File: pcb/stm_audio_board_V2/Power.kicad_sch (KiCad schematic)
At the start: 25 parts, among them J1 Power conn, U2 AMS1117-3.3, U4 OP275, U5 AMS1117-3.3, U7 OP275

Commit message: in_between_commit
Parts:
- removed H1, H2, H4: MountingHole_Pad, MountingHole:MountingHole_3.2mm_M3, symbol Mechanical:MountingHole_Pad
- added H3 (x3): MountingHole_Pad, MountingHole:MountingHole_3.2mm_M3_DIN965_Pad, symbol Mechanical:MountingHole_Pad
- H3: footprint MountingHole:MountingHole_3.2mm_M3 -> MountingHole:MountingHole_3.2mm_M3_DIN965_Pad
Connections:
- net GND: now also H3.1, H3.1, H3.1
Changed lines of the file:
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@@
     (stroke (width 0) (type default))
   )
-  (wire (pts (xy 43.18 143.51) (xy 45.72 143.51))
+  (wire (pts (xy 41.91 143.51) (xy 45.72 143.51))
     (stroke (width 0) (type default))
   )
@@
   (label "+9V" (at 135.89 48.26 180) (fields_autoplaced)
     (effects (font (size 1.27 1.27)) (justify right bottom))
-  )
-  (symbol (lib_id "Mechanical:MountingHole_Pad") (at 40.64 149.86 90) (unit 1)
-    (in_bom yes) (on_board yes) (dnp no) (fields_autoplaced)
-    (property "Reference" "H1" (at 39.37 144.78 90)
-      (effects (font (size 1.27 1.27)))
-    )
-    (property "Value" "MountingHole_Pad" (at 39.37 147.32 90)
-      (effects (font (size 1.27 1.27)))
-    )
-    (property "Footprint" "MountingHole:MountingHole_3.2mm_M3" (at 40.64 149.86 0)
-      (effects (font (size 1.27 1.27)) hide)
-    )
-    (property "Datasheet" "~" (at 40.64 149.86 0)
-      (effects (font (size 1.27 1.27)) hide)
-    )
-    (pin "1")
-    (instances
-      (project "stm_audio_board_V2"
-        (path "/6997cf63-2615-4e49-9471-e7da1b6bae71"
-          (reference "H1") (unit 1)
-        )
-        (path "/6997cf63-2615-4e49-9471-e7da1b6bae71/2eb2ee8f-ab98-4666-97f0-bfacb073bc88"
-          (reference "H3") (unit 1)
-        )
-      )
-    )
   )
   (symbol (lib_id "Connector_Generic:Conn_01x02") (at 27.94 44.45 180) (unit 1)
@@
     )
   )
+  (symbol (lib_id "Mechanical:MountingHole_Pad") (at 40.64 156.21 90) (unit 1)
+    (in_bom yes) (on_board yes) (dnp no) (fields_autoplaced)
+    (property "Reference" "H3" (at 39.37 151.13 90)
+      (effects (font (size 1.27 1.27)))
+    )
+    (property "Value" "MountingHole_Pad" (at 39.37 153.67 90)
+      (effects (font (size 1.27 1.27)))
+    )
+    (property "Footprint" "MountingHole:MountingHole_3.2mm_M3_DIN965_Pad" (at 40.64 156.21 0)
+      (effects (font (size 1.27 1.27)) hide)
+    )
+    (property "Datasheet" "~" (at 40.64 156.21 0)
+      (effects (font (size 1.27 1.27)) hide)
+    )
+    (pin "1")
+    (instances
+      (project "stm_audio_board_V2"
+        (path "/6997cf63-2615-4e49-9471-e7da1b6bae71"
+          (reference "H3") (unit 1)
+        )
+        (path "/6997cf63-2615-4e49-9471-e7da1b6bae71/2eb2ee8f-ab98-4666-97f0-bfacb073bc88"
+          (reference "H4") (unit 1)
+        )
+      )
+    )
+  )
   (symbol (lib_id "Regulator_Linear:AMS1117-3.3") (at 72.39 41.91 0) (unit 1)
     (in_bom yes) (on_board yes) (dnp no) (fields_autoplaced)
@@
         (path "/6997cf63-2615-4e49-9471-e7da1b6bae71/2eb2ee8f-ab98-4666-97f0-bfacb073bc88"
           (reference "U2") (unit 1)
+        )
+      )
+    )
+  )
+  (symbol (lib_id "Mechanical:MountingHole_Pad") (at 39.37 143.51 90) (unit 1)
+    (in_bom yes) (on_board yes) (dnp no) (fields_autoplaced)
+    (property "Reference" "H3" (at 38.1 138.43 90)
+      (effects (font (size 1.27 1.27)))
+    )
+    (property "Value" "MountingHole_Pad" (at 38.1 140.97 90)
+      (effects (font (size 1.27 1.27)))
+    )
+    (property "Footprint" "MountingHole:MountingHole_3.2mm_M3_DIN965_Pad" (at 39.37 143.51 0)
+      (effects (font (size 1.27 1.27)) hide)
+    )
+    (property "Datasheet" "~" (at 39.37 143.51 0)
+      (effects (font (size 1.27 1.27)) hide)
+    )
+    (pin "1")
+    (instances
+      (project "stm_audio_board_V2"
+        (path "/6997cf63-2615-4e49-9471-e7da1b6bae71"
+          (reference "H3") (unit 1)
+        )
+        (path "/6997cf63-2615-4e49-9471-e7da1b6bae71/2eb2ee8f-ab98-4666-97f0-bfacb073bc88"
+          (reference "H2") (unit 1)
         )
       )
@@
     )
   )
-  (symbol (lib_id "Mechanical:MountingHole_Pad") (at 40.64 143.51 90) (unit 1)
-    (in_bom yes) (on_board yes) (dnp no) (fields_autoplaced)
-    (property "Reference" "H2" (at 39.37 138.43 90)
-      (effects (font (size 1.27 1.27)))
-    )
-    (property "Value" "MountingHole_Pad" (at 39.37 140.97 90)
-      (effects (font (size 1.27 1.27)))
-    )
-    (property "Footprint" "MountingHole:MountingHole_3.2mm_M3" (at 40.64 143.51 0)
-      (effects (font (size 1.27 1.27)) hide)
-    )
-    (property "Datasheet" "~" (at 40.64 143.51 0)
-      (effects (font (size 1.27 1.27)) hide)
-    )
-    (pin "1")
-    (instances
-      (project "stm_audio_board_V2"
-        (path "/6997cf63-2615-4e49-9471-e7da1b6bae71"
-          (reference "H2") (unit 1)
-        )
-        (path "/6997cf63-2615-4e49-9471-e7da1b6bae71/2eb2ee8f-ab98-4666-97f0-bfacb073bc88"
-          (reference "H2") (unit 1)
+  (symbol (lib_id "Mechanical:MountingHole_Pad") (at 40.64 149.86 90) (unit 1)
+    (in_bom yes) (on_board yes) (dnp no) (fields_autoplaced)
+    (property "Reference" "H3" (at 39.37 144.78 90)
+      (effects (font (size 1.27 1.27)))
+    )
+    (property "Value" "MountingHole_Pad" (at 39.37 147.32 90)
+      (effects (font (size 1.27 1.27)))
+    )
+    (property "Footprint" "MountingHole:MountingHole_3.2mm_M3_DIN965_Pad" (at 40.64 149.86 0)
+      (effects (font (size 1.27 1.27)) hide)
+    )
+    (property "Datasheet" "~" (at 40.64 149.86 0)
+      (effects (font (size 1.27 1.27)) hide)
+    )
+    (pin "1")
+    (instances
+      (project "stm_audio_board_V2"
+        (path "/6997cf63-2615-4e49-9471-e7da1b6bae71"
+          (reference "H3") (unit 1)
+        )
+        (path "/6997cf63-2615-4e49-9471-e7da1b6bae71/2eb2ee8f-ab98-4666-97f0-bfacb073bc88"
+          (reference "H3") (unit 1)
         )
       )
@@
       (effects (font (size 1.27 1.27)))
     )
-    (property "Footprint" "MountingHole:MountingHole_3.2mm_M3" (at 40.64 138.43 0)
+    (property "Footprint" "MountingHole:MountingHole_3.2mm_M3_DIN965_Pad" (at 40.64 138.43 0)
       (effects (font (size 1.27 1.27)) hide)
     )
@@
         )
       )
-    )
-  )
-  (symbol (lib_id "Mechanical:MountingHole_Pad") (at 40.64 156.21 90) (unit 1)
-    (in_bom yes) (on_board yes) (dnp no) (fields_autoplaced)
-    (property "Reference" "H4" (at 39.37 151.13 90)
-      (effects (font (size 1.27 1.27)))
-    )
-    (property "Value" "MountingHole_Pad" (at 39.37 153.67 90)
-      (effects (font (size 1.27 1.27)))
-    )
-    (property "Footprint" "MountingHole:MountingHole_3.2mm_M3" (at 40.64 156.21 0)
-      (effects (font (size 1.27 1.27)) hide)
-    )
-    (property "Datasheet" "~" (at 40.64 156.21 0)
-      (effects (font (size 1.27 1.27)) hide)
-    )
-    (pin "1")
-    (instances
-      (project "stm_audio_board_V2"
-        (path "/6997cf63-2615-4e49-9471-e7da1b6bae71"
-          (reference "H4") (unit 1)
-        )
-        (path "/6997cf63-2615-4e49-9471-e7da1b6bae71/2eb2ee8f-ab98-4666-97f0-bfacb073bc88"
-          (reference "H4") (unit 1)
-        )
-      )

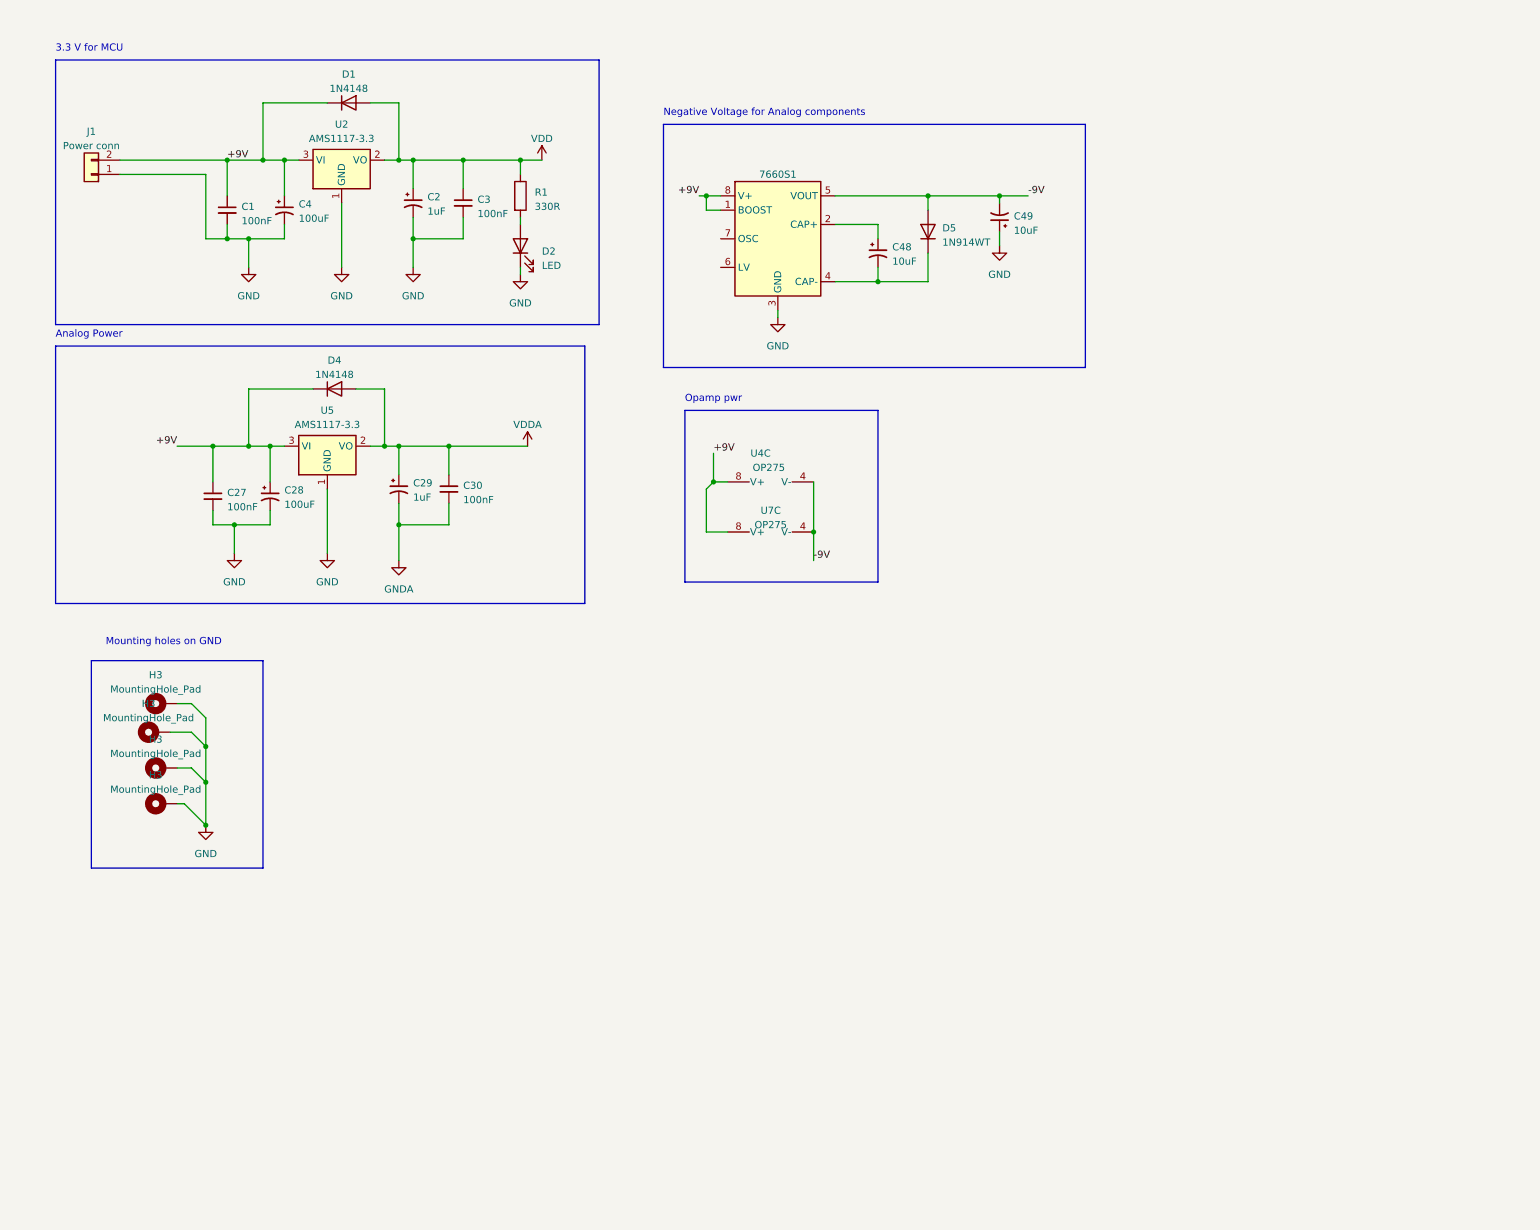
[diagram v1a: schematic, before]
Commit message: added choke to analog pwr, created 5 V rail, decided to pivot and use codec instead dedicated hardware
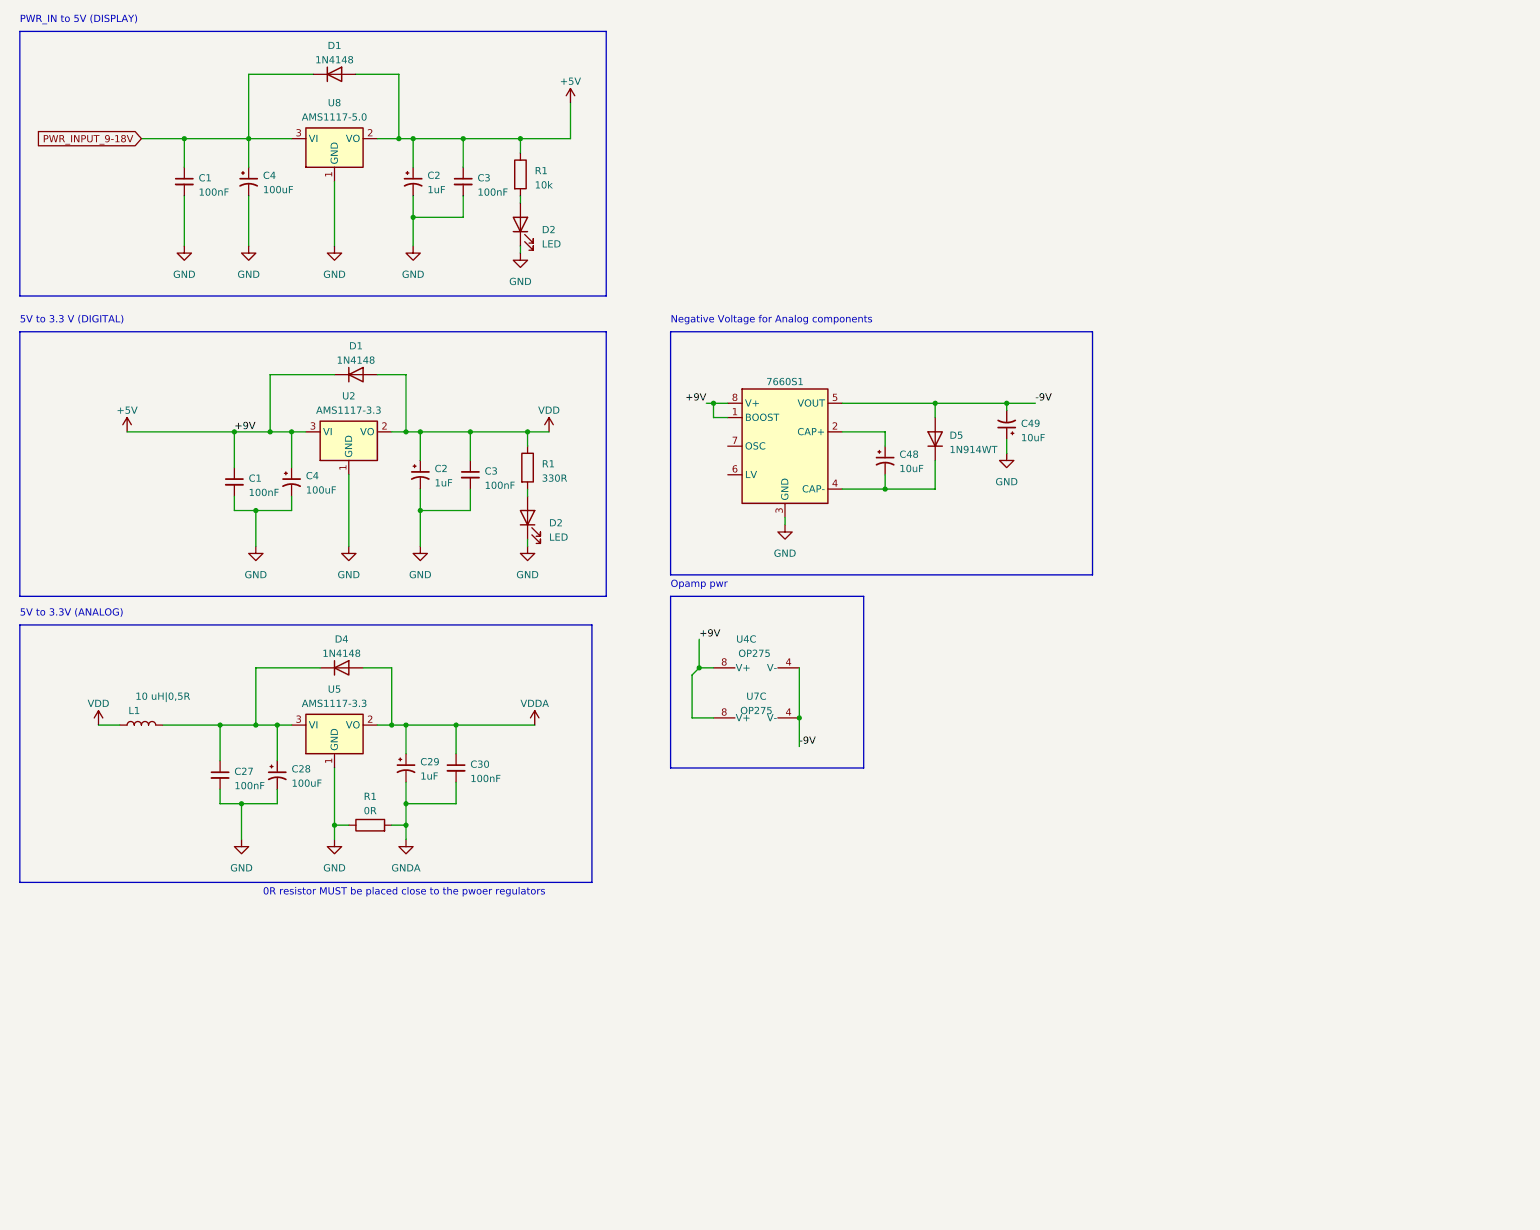
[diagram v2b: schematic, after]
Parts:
- removed H3 (x4): MountingHole_Pad, MountingHole:MountingHole_3.2mm_M3_DIN965_Pad, symbol Mechanical:MountingHole_Pad
- removed J1: Power conn, Connector_PinHeader_2.54mm:PinHeader_1x02_P2.54mm_Vertical, symbol Connector_Generic:Conn_01x02
- added C1, C3: 100nF, Capacitor_SMD:C_0603_1608Metric_Pad1.08x0.95mm_HandSolder, symbol Device:C_Small
- added C2: 1uF, Capacitor_THT:CP_Radial_D6.3mm_P2.50mm, symbol Device:C_Polarized_Small_US
- added C4: 100uF, Capacitor_THT:CP_Radial_D6.3mm_P2.50mm, symbol Device:C_Polarized_Small_US
- added D1: 1N4148, Diode_THT:D_DO-35_SOD27_P7.62mm_Horizontal, symbol Diode:1N4148
- added D2: LED, LED_SMD:LED_SK6805_PLCC4_2.4x2.7mm_P1.3mm, symbol Device:LED
- added L1: 10 uH|0,5R, Inductor_THT:L_Axial_L9.5mm_D4.0mm_P12.70mm_Horizontal_Fastron_SMCC, symbol Device:L
- added R1: 0R, Resistor_SMD:R_0805_2012Metric_Pad1.20x1.40mm_HandSolder, symbol Device:R
- added R1: 10k, Resistor_SMD:R_0805_2012Metric_Pad1.20x1.40mm_HandSolder, symbol Device:R
- added U8: AMS1117-5.0, Package_TO_SOT_SMD:SOT-223-3_TabPin2, symbol Regulator_Linear:AMS1117-5.0
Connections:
- net GND: now also C1.2, C2.2, C3.2, C4.2, D2.1 (K), R1.1, U8.1 (GND)
- net GNDA: now also R1.2
- net VDD: now also L1.1
- net +9V renamed +5V
- net +5V: now also C2.1, C3.1, D1.2 (A), R1.1, U8.2 (VO); no longer C27.1, C28.1, D4.1 (K), U5.3 (VI)
- new net: D2.2 (A), R1.2
- new net: C27.1, C28.1, D4.1 (K), L1.2, U5.3 (VI)
- new net PWR_INPUT_9-18V: C1.1, C4.1, D1.1 (K), U8.3 (VI)
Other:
- note added: "0R resistor MUST be placed close to the pwoer regulators"
- note added: "5V to 3.3 V (DIGITAL)"
- note added: "5V to 3.3V (ANALOG)"
- note added: "PWR_IN to 5V (DISPLAY)"
- note removed: "3.3 V for MCU"
- note removed: "Analog Power"
- note removed: "Mounting holes on GND"
- moved on the sheet: 7660S1, C1, C2, C27, C28, C29, C3, C30, C4, C48, C49, D1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

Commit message: Update AD1939_input_with_offset.asc, AD1939_input_with_offset.net, and 6 more files...
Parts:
- removed 7660S1: ~, Package_SO:SOIC-8_3.9x4.9mm_P1.27mm, symbol stm_audio:7660S
- removed C48: 10uF, Capacitor_THT:CP_Radial_D6.3mm_P2.50mm, symbol Device:C_Polarized_Small_US
- removed C49: 10uF, Capacitor_SMD:C_1210_3225Metric_Pad1.33x2.70mm_HandSolder, symbol Device:C_Polarized_Small_US
- removed D5: 1N914WT, Diode_SMD:D_SOD-523, symbol Diode:1N914WT
- removed R1: 0R, Resistor_SMD:R_0805_2012Metric_Pad1.20x1.40mm_HandSolder, symbol Device:R
- added C1, C3: 100nF, Capacitor_SMD:C_0603_1608Metric_Pad1.08x0.95mm_HandSolder, symbol Device:C_Small
- added C2: 1uF, Capacitor_THT:CP_Radial_D6.3mm_P2.50mm, symbol Device:C_Polarized_Small_US
- added C4: 100uF, Capacitor_THT:CP_Radial_D6.3mm_P2.50mm, symbol Device:C_Polarized_Small_US
- added D1: 1N4148, Diode_THT:D_DO-35_SOD27_P7.62mm_Horizontal, symbol Diode:1N4148
- added D2: LED, LED_SMD:LED_SK6805_PLCC4_2.4x2.7mm_P1.3mm, symbol Device:LED
- added L2: 10 uH|0,5R, Inductor_THT:L_Axial_L9.5mm_D4.0mm_P12.70mm_Horizontal_Fastron_SMCC, symbol Device:L
- added R1: 10k, Resistor_SMD:R_0805_2012Metric_Pad1.20x1.40mm_HandSolder, symbol Device:R
- added R1: 0R, Resistor_SMD:R_0805_2012Metric_Pad1.20x1.40mm_HandSolder, symbol Device:R
- added U9: L7809, Package_TO_SOT_THT:TO-220-3_Horizontal_TabDown, symbol Regulator_Linear:L7809
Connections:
- net -9V is gone; now on net GNDA: U4.4 (V-), U7.4 (V-)
- net +5V: now also L1.1; no longer U4.8 (V+), U7.8 (V+)
- net GND: now also C1.2, C2.2, C3.2, C4.2, D2.1 (K), U9.2 (GND); no longer C27.2, C28.2, U5.1 (GND)
- net GNDA: now also C27.2, C28.2, U5.1 (GND), R1.1, R1.2
- net VDD: no longer L1.1
- net PWR_INPUT_9-18V renamed +9V
- net +9V: now also C2.1, C3.1, D1.2 (A), R1.1, U9.3 (OUT)
- new net: C1.1, C4.1, D1.1 (K), L2.2, U9.1 (IN)
- new net: U4.8 (V+), U7.8 (V+)
- new net: D2.2 (A), R1.2
- new net PWR_INPUT_12V-18V: L2.1
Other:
- note added: "9V to 5V (DISPLAY)"
- note added: "PWR_IN to 9V (DISPLAY)"
- note removed: "Negative Voltage for Analog components"
- note removed: "PWR_IN to 5V (DISPLAY)"
- moved on the sheet: C1, C2, C3, C4, D1, D2, R1, U8

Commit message: Update AD1939_input_with_offset.asc, AD1939_input_with_offset.log, and 8 more files...
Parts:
- removed R1: 0R, Resistor_SMD:R_0805_2012Metric_Pad1.20x1.40mm_HandSolder, symbol Device:R
- added 7660S1: ~, symbol stm_audio:7660S
- added C2 (x2): 10uF, Capacitor_THT:CP_Radial_D6.3mm_P2.50mm, symbol Device:C_Polarized_Small_US
- added U10: TL072, symbol Amplifier_Operational:TL072
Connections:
- net +9V: now also U4.8 (V+), U7.8 (V+), 7660S1.1 (BOOST), 7660S1.8 (V+), U10.8 (V+)
- net GND: now also C27.2, C28.2, C29.2, C30.2, U5.1 (GND), 7660S1.3 (GND), C2.1, U10.4 (V-)
- removed net GNDA: C27.2, C28.2, C29.2, C30.2, U4.4 (V-), U5.1 (GND), U7.4 (V-)
- new net: 7660S1.2 (CAP+), C2.1
- new net: 7660S1.4 (CAP-), C2.2
- new net -9V: 7660S1.5 (VOUT), C2.2, U4.4 (V-), U7.4 (V-)
